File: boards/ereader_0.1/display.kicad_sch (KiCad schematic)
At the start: 18 parts, among them P1 FPC24, Q1 Si1308EDL

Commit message: finished bom
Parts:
- C1, C7: value 1uf/25V -> 1u/25v
- C2: value 1u/10v -> 1u/25v
- C34: value 1u/10V -> 1u/25v
- R2: value 0.47r -> 0R47
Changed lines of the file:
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@@
 		(dnp no)
 		(property "Reference" "C2"
-			(at 92.456 58.166 90)
-			(show_name no)
-			(do_not_autoplace no)
-			(effects
-				(font
-					(size 1.27 1.27)
-				)
-			)
-		)
-		(property "Value" "1u/10v"
+			(at 91.948 58.166 90)
+			(show_name no)
+			(do_not_autoplace no)
+			(effects
+				(font
+					(size 1.27 1.27)
+				)
+			)
+		)
+		(property "Value" "1u/25v"
 			(at 101.092 58.166 90)
 			(show_name no)
@@
 		(dnp no)
 		(property "Reference" "C4"
-			(at 92.456 68.326 90)
+			(at 91.948 68.326 90)
 			(show_name no)
 			(do_not_autoplace no)
@@
 			)
 		)
-		(property "Value" "0.47r"
+		(property "Value" "0R47"
 			(at 46.99 73.6599 0)
 			(show_name no)
@@
 		(dnp no)
 		(property "Reference" "C3"
-			(at 92.456 63.246 90)
+			(at 91.948 63.246 90)
 			(show_name no)
 			(do_not_autoplace no)
@@
 			)
 		)
-		(property "Value" "1uf/25V"
+		(property "Value" "1u/25v"
 			(at 114.3 87.6299 0)
 			(show_name no)
@@
 			)
 		)
-		(property "Value" "1u/10V"
+		(property "Value" "1u/25v"
 			(at 25.4 55.8799 0)
 			(show_name no)
@@
 		(dnp no)
 		(property "Reference" "C1"
-			(at 114.046 30.226 90)
-			(show_name no)
-			(do_not_autoplace no)
-			(effects
-				(font
-					(size 1.27 1.27)
-				)
-			)
-		)
-		(property "Value" "1uf/25V"
+			(at 113.538 30.226 90)
+			(show_name no)
+			(do_not_autoplace no)
+			(effects
+				(font
+					(size 1.27 1.27)
+				)
+			)
+		)
+		(property "Value" "1u/25v"
 			(at 122.682 30.226 90)
 			(show_name no)
@@
 		(dnp no)
 		(property "Reference" "C5"
-			(at 92.456 73.406 90)
-			(show_name no)
-			(do_not_autoplace no)
+			(at 91.948 73.406 90)
+			(show_name no)
+			(do_not_autoplace no)

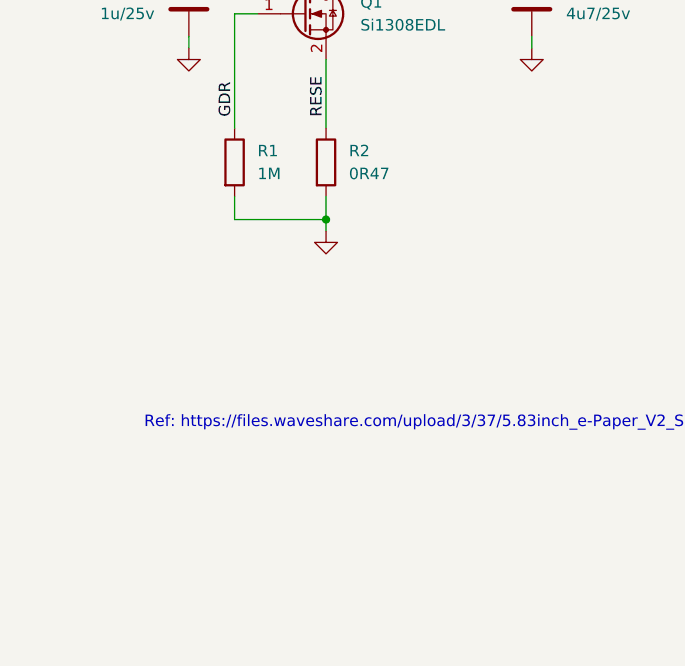
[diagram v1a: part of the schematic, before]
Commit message: add bringup test
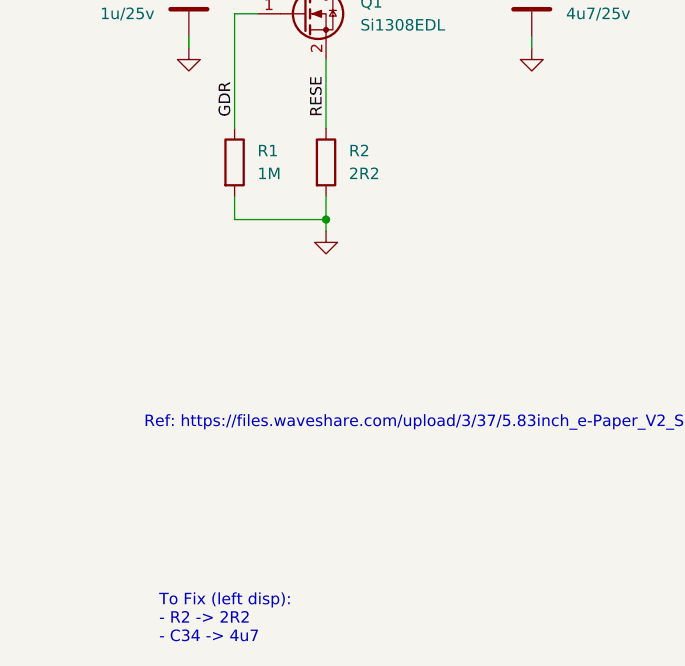
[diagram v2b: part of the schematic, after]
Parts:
- R2: value 0R47 -> 2R2
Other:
- note added: "To Fix (left disp): - R2 -> 2R2 - C34 -> 4u7"
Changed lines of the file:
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@@
 	(generator_version "10.0")
 	(paper "A4")
+	(text "To Fix (left disp):\n- R2 -> 2R2\n- C34 -> 4u7\n"
+		(exclude_from_sim no)
+		(at 25.908 123.19 0)
+		(effects
+			(font
+				(size 1.27 1.27)
+			)
+			(justify left)
+		)
+	)
 	(text "Ref: https://files.waveshare.com/upload/3/37/5.83inch_e-Paper_V2_Specification.pdf"
 		(exclude_from_sim no)
@@
 			)
 		)
-		(property "Value" "0R47"
+		(property "Value" "2R2"
 			(at 46.99 73.6599 0)
 			(show_name no)
